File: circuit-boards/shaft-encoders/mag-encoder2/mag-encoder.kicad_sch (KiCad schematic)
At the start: 22 parts, among them J1 CONFIG, J2 0015912055, Q1 BSS84, U1 AP2120N-3.3TRG1, U2 MA732GQ

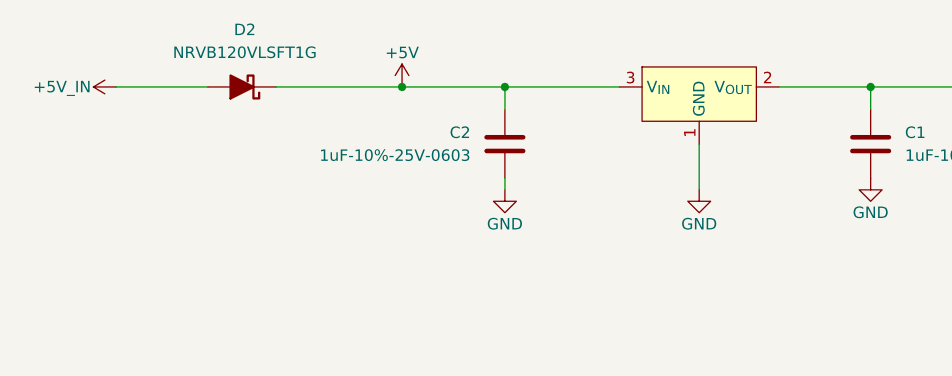
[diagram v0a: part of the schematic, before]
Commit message: Changed power LED to yellow. Reverse polarity diode to 1N4148
Signed-off-by: Scott <sgberman1@gmail.com>
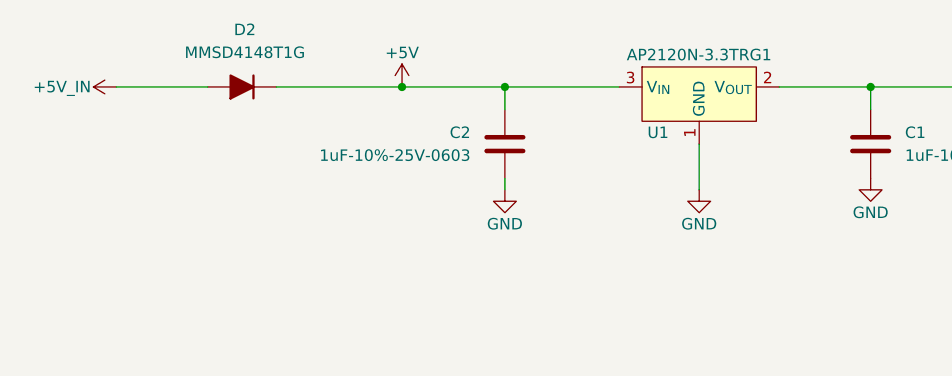
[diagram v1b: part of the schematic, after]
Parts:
- D1: DIST P/N 732-4971-1-ND -> 732-4981-1-ND; MFG P/N 150060GS75000 -> 150060YS75000
- D2: value NRVB120VLSFT1G -> MMSD4148T1G; footprint Diode_SMD:D_SOD-123F -> Diode_SMD:D_SOD-123; DIST P/N NRVB120VLSFT1GOSCT-ND -> MMSD4148T1GOSCT-ND; MFG P/N NRVB120VLSFT1G -> MMSD4148T1G
- D4: DIST P/N 732-4971-1-ND -> 732-4980-1-ND; MFG P/N 150060GS75000 -> 150060VS75000
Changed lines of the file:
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@@
 	(title_block
 		(title "Mag Encoder")
-		(date "2024-08-25")
-		(rev "1")
+		(date "2024-08-31")
+		(rev "2")
 		(company "971 SPARTAN ROBOTICS")
 	)
@@
 			)
 		)
-		(property "Value" "NRVB120VLSFT1G"
+		(property "Value" "MMSD4148T1G"
 			(at 67.6275 44.45 0)
 			(effects
@@
 			)
 		)
-		(property "Footprint" "Diode_SMD:D_SOD-123F"
+		(property "Footprint" "Diode_SMD:D_SOD-123"
 			(at 67.31 48.26 0)
 			(effects
@@
 			)
 		)
-		(property "Datasheet" "Components/onsemi-MBR120VLSF.pdf"
+		(property "Datasheet" "Components/onsemi-MMSD4148T1-D.PDF"
 			(at 67.31 48.26 0)
 			(effects
@@
 			)
 		)
-		(property "Description" "Diode Schottky 20 V 1A Surface Mount SOD-123FL"
+		(property "Description" "Diode 100 V 200mA Surface Mount SOD-123"
 			(at 67.31 48.26 0)
 			(effects
@@
 			)
 		)
-		(property "MFG P/N" "NRVB120VLSFT1G"
+		(property "MFG P/N" "MMSD4148T1G"
 			(at 67.31 48.26 0)
 			(effects
@@
 			)
 		)
-		(property "DIST P/N" "NRVB120VLSFT1GOSCT-ND"
+		(property "DIST P/N" "MMSD4148T1GOSCT-ND"
 			(at 67.31 48.26 0)
 			(effects
@@
 		(on_board yes)
 		(dnp no)
-		(fields_autoplaced yes)
 		(property "Reference" "U1"
-			(at 118.11 45.72 0)
+			(at 113.538 53.34 0)
 			(effects
 				(font
 					(size 1.27 1.27)
 				)
-				(hide yes)
 			)
 		)
 		(property "Value" "AP2120N-3.3TRG1"
-			(at 118.11 45.72 0)
+			(at 118.11 44.704 0)
 			(effects
 				(font
 					(size 1.27 1.27)
 				)
-				(hide yes)
 			)
 		)
@@
 			)
 		)
-		(property "Datasheet" "Components/Wurth-150060GS75000.pdf"
+		(property "Datasheet" "Components/Wurth-150060VS75000.pdf"
 			(at 252.73 167.64 0)
 			(effects
@@
 			)
 		)
-		(property "MFG P/N" "150060GS75000"
+		(property "MFG P/N" "150060VS75000"
 			(at 252.73 167.64 0)
 			(effects
@@
 			)
 		)
-		(property "DIST P/N" "732-4971-1-ND"
+		(property "DIST P/N" "732-4980-1-ND"
 			(at 252.73 167.64 0)
 			(effects
@@
 	)
 	(symbol
+		(lib_name "LED_3")
 		(lib_id "Device:LED")
 		(at 171.45 53.34 90)
@@
 			)
 		)
-		(property "Datasheet" "Components/Wurth-150060GS75000.pdf"
+		(property "Datasheet" "Components/Wurth-150060YS75000.pdf"
 			(at 171.45 53.34 0)
 			(effects
@@
 			)
 		)
-		(property "MFG P/N" "150060GS75000"
+		(property "MFG P/N" "150060YS75000"
 			(at 171.45 53.34 0)
 			(effects
@@
 			)
 		)
-		(property "DIST P/N" "732-4971-1-ND"
+		(property "DIST P/N" "732-4981-1-ND"
 			(at 171.45 53.34 0)
 			(effects
